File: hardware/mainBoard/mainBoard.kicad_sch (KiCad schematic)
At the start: 17 parts, among them J1 DisplayConnector, J2 LeftKeyConnector, J3 RightKeyConnector, J4 EncoderConnector

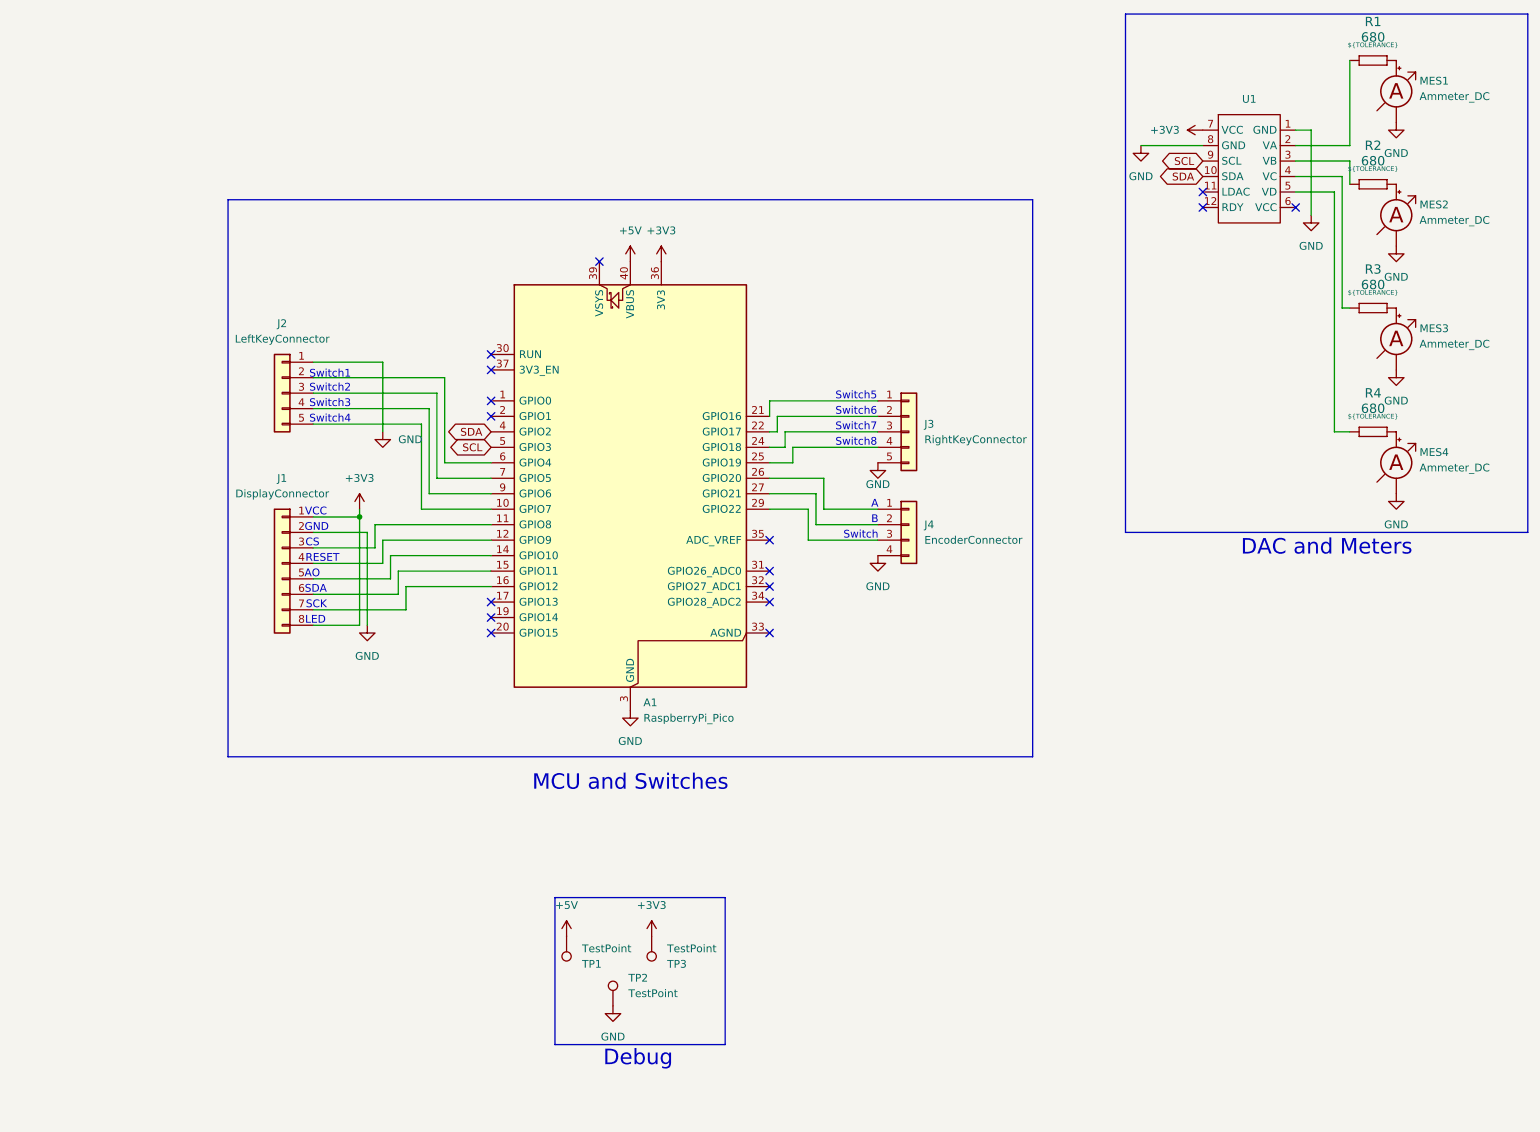
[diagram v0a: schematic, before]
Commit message: Switched from prebuilt module to chip
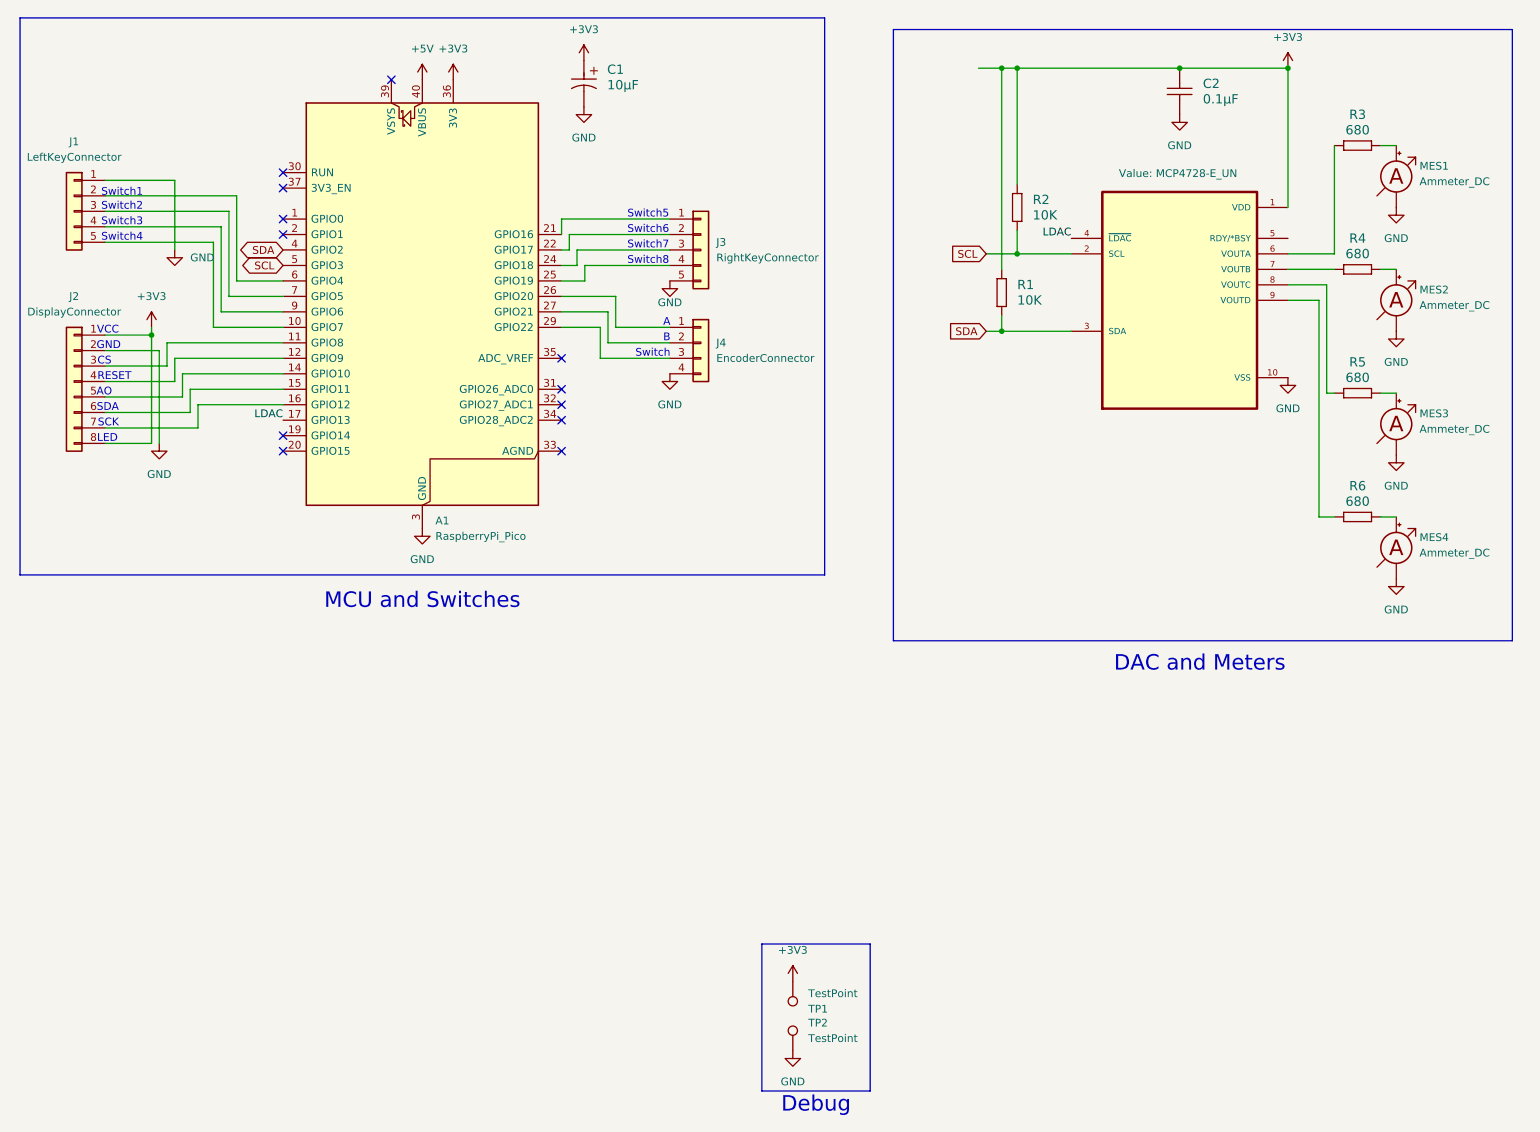
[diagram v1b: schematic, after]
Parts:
- removed R1, R2, R3, R4: 680, Resistor_THT:R_Axial_DIN0207_L6.3mm_D2.5mm_P7.62mm_Horizontal, symbol Resistors:Resistor - 1%
- removed TP1: TestPoint, TestPoint:TestPoint_Pad_D2.5mm, symbol Connector:TestPoint
- removed U1: (no value), Adafruit_MCP4728:Adafruit_MCP4728, symbol Adafruit_MCP4728:Adafruit_MCP4728
- added C1: 10µF, Capacitor_Tantalum_SMD:CP_EIA-3528-15_AVX-H_HandSolder, symbol Capacitors:Capacitor - polarized
- added C2: 0.1μF, Capacitor_SMD:C_1206_3216Metric_Pad1.33x1.80mm_HandSolder, symbol Capacitors:Capacitor - non polarized
- added R1, R2: 10K, Resistor_SMD:R_1206_3216Metric_Pad1.30x1.75mm_HandSolder, symbol Resistors:Resistor
- added R3, R4, R5, R6: 680, Resistor_SMD:R_1206_3216Metric_Pad1.30x1.75mm_HandSolder, symbol Resistors:Resistor
- added U1: MCP4728-E_UN, Snapeda:SOP50P490X110-10N, symbol Snapeda:MCP4728-E_UN
- renumbered J2 to J1, J1 to J2, TP3 to TP1
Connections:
- net +3V3: now also C1.1, C2.1, R1.1, R2.1, U1.1 (VDD)
- net GND: now also C1.2, C2.2, U1.10 (VSS)
- net SCL: now also R2.2, U1.2 (SCL)
- net SDA: now also R1.2, U1.3 (SDA)
- net LDAC: now reaches A1.17 (GPIO13)
- net LDAC: now also U1.4 (~{LDAC})
- net at MES2.2 (+): now also R4.2
- net at MES4.2 (+): now also R6.2
- net at MES1.2 (+): now also R3.2
- net at MES3.2 (+): now also R5.2
- new net: R6.1, U1.9 (VOUTD)
- new net: R4.1, U1.7 (VOUTB)
- new net: R5.1, U1.8 (VOUTC)
- new net: R3.1, U1.6 (VOUTA)
- no-connect marks 16 -> 12
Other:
- moved on the sheet: A1, J1, J2, J3, J4, MES1, MES2, MES3, MES4, TP1, TP2

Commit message: Label the connectors in the silkscreen
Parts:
- removed TP1, TP2: TestPoint, TestPoint:TestPoint_Pad_D2.5mm, symbol Connector:TestPoint
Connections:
- no-connect marks 12 -> 13
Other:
- note removed: "Debug"
- moved on the sheet: A1, J1, J2, J3, J4

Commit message: update PCB routing and add debug probe
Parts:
- added J1: UARTDebug, Connector_JST:JST_XH_B4B-XH-A_1x04_P2.50mm_Vertical, symbol Connector_Generic:Conn_01x04
- C2: value 0.1μF -> 100nF
- renumbered J1 to J2, J2 to J3, J3 to J4, J4 to J5
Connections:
- net +3V3: now also J3.2 (Pin_2), J1.1 (Pin_1); no longer J3.1 (Pin_1)
- net GND: now also J3.1 (Pin_1), J1.4 (Pin_4); no longer J3.2 (Pin_2)
- net at A1.1 (GPIO0): now also J1.2 (Pin_2)
- net at A1.2 (GPIO1): now also J1.3 (Pin_3)
- no-connect marks 13 -> 11
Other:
- note added: "DC"
- note added: "RX"
- note added: "TX"
- note removed: "AO"

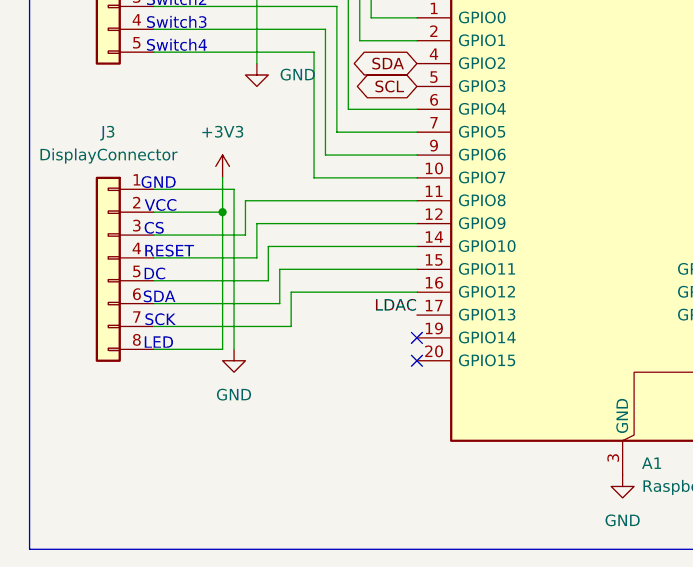
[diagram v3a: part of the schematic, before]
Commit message: update wiring
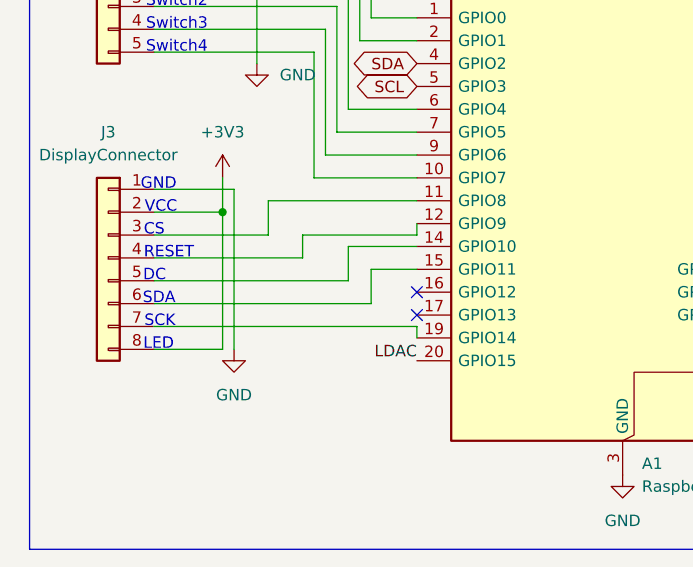
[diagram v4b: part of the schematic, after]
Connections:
- net LDAC: now also A1.20 (GPIO15); no longer A1.17 (GPIO13)
- net at A1.16 (GPIO12): no longer J3.7 (Pin_7)
- net at A1.19 (GPIO14): now also J3.7 (Pin_7)
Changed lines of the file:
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@@
-	)
-	(no_connect
-		(at 64.77 83.82)
 	)
 	(no_connect
@@
 	)
 	(no_connect
-		(at 64.77 86.36)
+		(at 64.77 78.74)
+	)
+	(no_connect
+		(at 64.77 81.28)
 	)
 	(wire
@@
 	(wire
 		(pts
+			(xy 64.77 72.39) (xy 64.77 71.12)
+		)
+		(stroke
+			(width 0)
+			(type default)
+		)
+	)
+	(wire
+		(pts
 			(xy 212.09 24.13) (xy 229.87 24.13)
 		)
@@
 	(wire
 		(pts
+			(xy 57.15 77.47) (xy 35.56 77.47)
+		)
+		(stroke
+			(width 0)
+			(type default)
+		)
+	)
+	(wire
+		(pts
 			(xy 247.65 97.79) (xy 245.11 97.79)
 		)
@@
 	(wire
 		(pts
+			(xy 48.26 72.39) (xy 48.26 68.58)
+		)
+		(stroke
+			(width 0)
+			(type default)
+		)
+	)
+	(wire
+		(pts
+			(xy 64.77 82.55) (xy 64.77 83.82)
+		)
+		(stroke
+			(width 0)
+			(type default)
+		)
+	)
+	(wire
+		(pts
 			(xy 185.42 50.8) (xy 185.42 54.61)
 		)
@@
 	(wire
 		(pts
-			(xy 49.53 76.2) (xy 49.53 80.01)
-		)
-		(stroke
-			(width 0)
-			(type default)
-		)
-	)
-	(wire
-		(pts
 			(xy 110.49 60.96) (xy 119.38 60.96)
 		)
@@
 	(wire
 		(pts
-			(xy 46.99 71.12) (xy 64.77 71.12)
-		)
-		(stroke
-			(width 0)
-			(type default)
-		)
-	)
-	(wire
-		(pts
 			(xy 237.49 54.61) (xy 237.49 36.83)
 		)
@@
 	(wire
 		(pts
+			(xy 52.07 72.39) (xy 64.77 72.39)
+		)
+		(stroke
+			(width 0)
+			(type default)
+		)
+	)
+	(wire
+		(pts
 			(xy 57.15 58.42) (xy 64.77 58.42)
 		)
@@
 	(wire
 		(pts
+			(xy 35.56 74.93) (xy 52.07 74.93)
+		)
+		(stroke
+			(width 0)
+			(type default)
+		)
+	)
+	(wire
+		(pts
 			(xy 110.49 48.26) (xy 110.49 50.8)
 		)
@@
 	(wire
 		(pts
+			(xy 64.77 73.66) (xy 57.15 73.66)
+		)
+		(stroke
+			(width 0)
+			(type default)
+		)
+	)
+	(wire
+		(pts
 			(xy 57.15 44.45) (xy 57.15 58.42)
 		)
@@
 	(wire
 		(pts
-			(xy 50.8 78.74) (xy 64.77 78.74)
-		)
-		(stroke
-			(width 0)
-			(type default)
-		)
-	)
-	(wire
-		(pts
-			(xy 46.99 74.93) (xy 46.99 71.12)
-		)
-		(stroke
-			(width 0)
-			(type default)
-		)
-	)
-	(wire
-		(pts
 			(xy 116.84 71.12) (xy 128.27 71.12)
 		)
@@
 	(wire
 		(pts
-			(xy 48.26 73.66) (xy 64.77 73.66)
-		)
-		(stroke
-			(width 0)
-			(type default)
-		)
-	)
-	(wire
-		(pts
-			(xy 64.77 76.2) (xy 49.53 76.2)
+			(xy 35.56 82.55) (xy 64.77 82.55)
 		)
 		(stroke
@@
 	(wire
 		(pts
-			(xy 35.56 72.39) (xy 45.72 72.39)
+			(xy 35.56 80.01) (xy 59.69 80.01)
 		)
 		(stroke
@@
 	(wire
 		(pts
-			(xy 50.8 82.55) (xy 50.8 78.74)
+			(xy 52.07 72.39) (xy 52.07 74.93)
+		)
+		(stroke
+			(width 0)
+			(type default)
+		)
+	)
+	(wire
+		(pts
+			(xy 64.77 76.2) (xy 59.69 76.2)
 		)
 		(stroke
@@
 	(wire
 		(pts
-			(xy 48.26 77.47) (xy 48.26 73.66)
-		)
-		(stroke
-			(width 0)
-			(type default)
-		)
-	)
-	(wire
-		(pts
 			(xy 229.87 57.15) (xy 237.49 57.15)
 		)
@@
 	(wire
 		(pts
-			(xy 45.72 68.58) (xy 64.77 68.58)
-		)
-		(stroke
-			(width 0)
-			(type default)
-		)
-	)
-	(wire
-		(pts
-			(xy 45.72 72.39) (xy 45.72 68.58)
-		)
-		(stroke
-			(width 0)
-			(type default)
-		)
-	)
-	(wire
-		(pts
-			(xy 35.56 82.55) (xy 50.8 82.55)
-		)
-		(stroke
-			(width 0)
-			(type default)
-		)
-	)
-	(wire
-		(pts
-			(xy 35.56 74.93) (xy 46.99 74.93)
-		)
-		(stroke
-			(width 0)
-			(type default)
-		)
-	)
-	(wire
-		(pts
 			(xy 182.88 57.15) (xy 182.88 24.13)
 		)
@@
 	(wire
 		(pts
+			(xy 48.26 68.58) (xy 64.77 68.58)
+		)
+		(stroke
+			(width 0)
+			(type default)
+		)
+	)
+	(wire
+		(pts
 			(xy 118.11 63.5) (xy 110.49 63.5)
 		)
@@
 	(wire
 		(pts
+			(xy 59.69 76.2) (xy 59.69 80.01)
+		)
+		(stroke
+			(width 0)
+			(type default)
+		)
+	)
+	(wire
+		(pts
 			(xy 44.45 67.31) (xy 44.45 85.09)
 		)
@@
 	(wire
 		(pts
-			(xy 35.56 77.47) (xy 48.26 77.47)
-		)
-		(stroke
-			(width 0)
-			(type default)
-		)
-	)
-	(wire
-		(pts
 			(xy 180.34 67.31) (xy 182.88 67.31)
 		)
@@
 	(wire
 		(pts
-			(xy 49.53 80.01) (xy 35.56 80.01)
+			(xy 57.15 73.66) (xy 57.15 77.47)
 		)
 		(stroke
@@
 	(wire
 		(pts
+			(xy 35.56 72.39) (xy 48.26 72.39)
+		)
+		(stroke
+			(width 0)
+			(type default)
+		)
+	)
+	(wire
+		(pts
 			(xy 35.56 25.4) (xy 59.69 25.4)
 		)
@@
 	)
 	(label "LDAC"
-		(at 64.77 81.28 180)
+		(at 64.77 86.36 180)
 		(effects
 			(font
